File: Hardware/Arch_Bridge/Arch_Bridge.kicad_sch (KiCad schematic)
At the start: 87 parts, among them J1 Conn_01x02, J3 Conn_01x04, J4 Conn_01x04, Q1 2N3904, Q2 MJE2955, Q3 MJE2955, U1 AP63205WU, U11 ESP32-S3-WROOM-1, U12 TXS0102DCT, U13 DRV8231ADDAR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

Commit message: Fixed R11 value, 33k => 3k so that Q2 sources correctly. Tested at 14.5mA on a 12v supply.
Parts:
- R11: value 33k -> 3k; PN RC1206FR-0733KL -> RC1206FR-073KL
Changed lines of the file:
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@@
       (effects (font (size 1.27 1.27)) (justify left))
     )
-    (property "Value" "33k" (at 31.75 168.91 90)
+    (property "Value" "3k" (at 31.75 168.91 90)
       (effects (font (size 1.27 1.27)) (justify left))
     )
@@
       (effects (font (size 1.27 1.27)) hide)
     )
-    (property "PN" "RC1206FR-0733KL" (at 32.385 167.005 0)
+    (property "PN" "RC1206FR-073KL" (at 32.385 167.005 0)
       (effects (font (size 1.27 1.27)) hide)
     )

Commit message: Adjusted R15 value and ADC code to make railsync current source work correctly. 0-208mA availabe.
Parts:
- R15: value 3k -> 470; PN RC1206FR-073KL -> RT1206FRE07470RL
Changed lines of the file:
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@@
       (effects (font (size 1.27 1.27)) (justify left))
     )
-    (property "Value" "3k" (at 185.42 92.71 90)
+    (property "Value" "470" (at 185.42 92.71 90)
       (effects (font (size 1.27 1.27)) (justify left))
     )
@@
       (effects (font (size 1.27 1.27)) hide)
     )
-    (property "PN" "RC1206FR-073KL" (at 182.88 90.17 0)
+    (property "PN" "RT1206FRE07470RL" (at 182.88 90.17 0)
       (effects (font (size 1.27 1.27)) hide)
     )

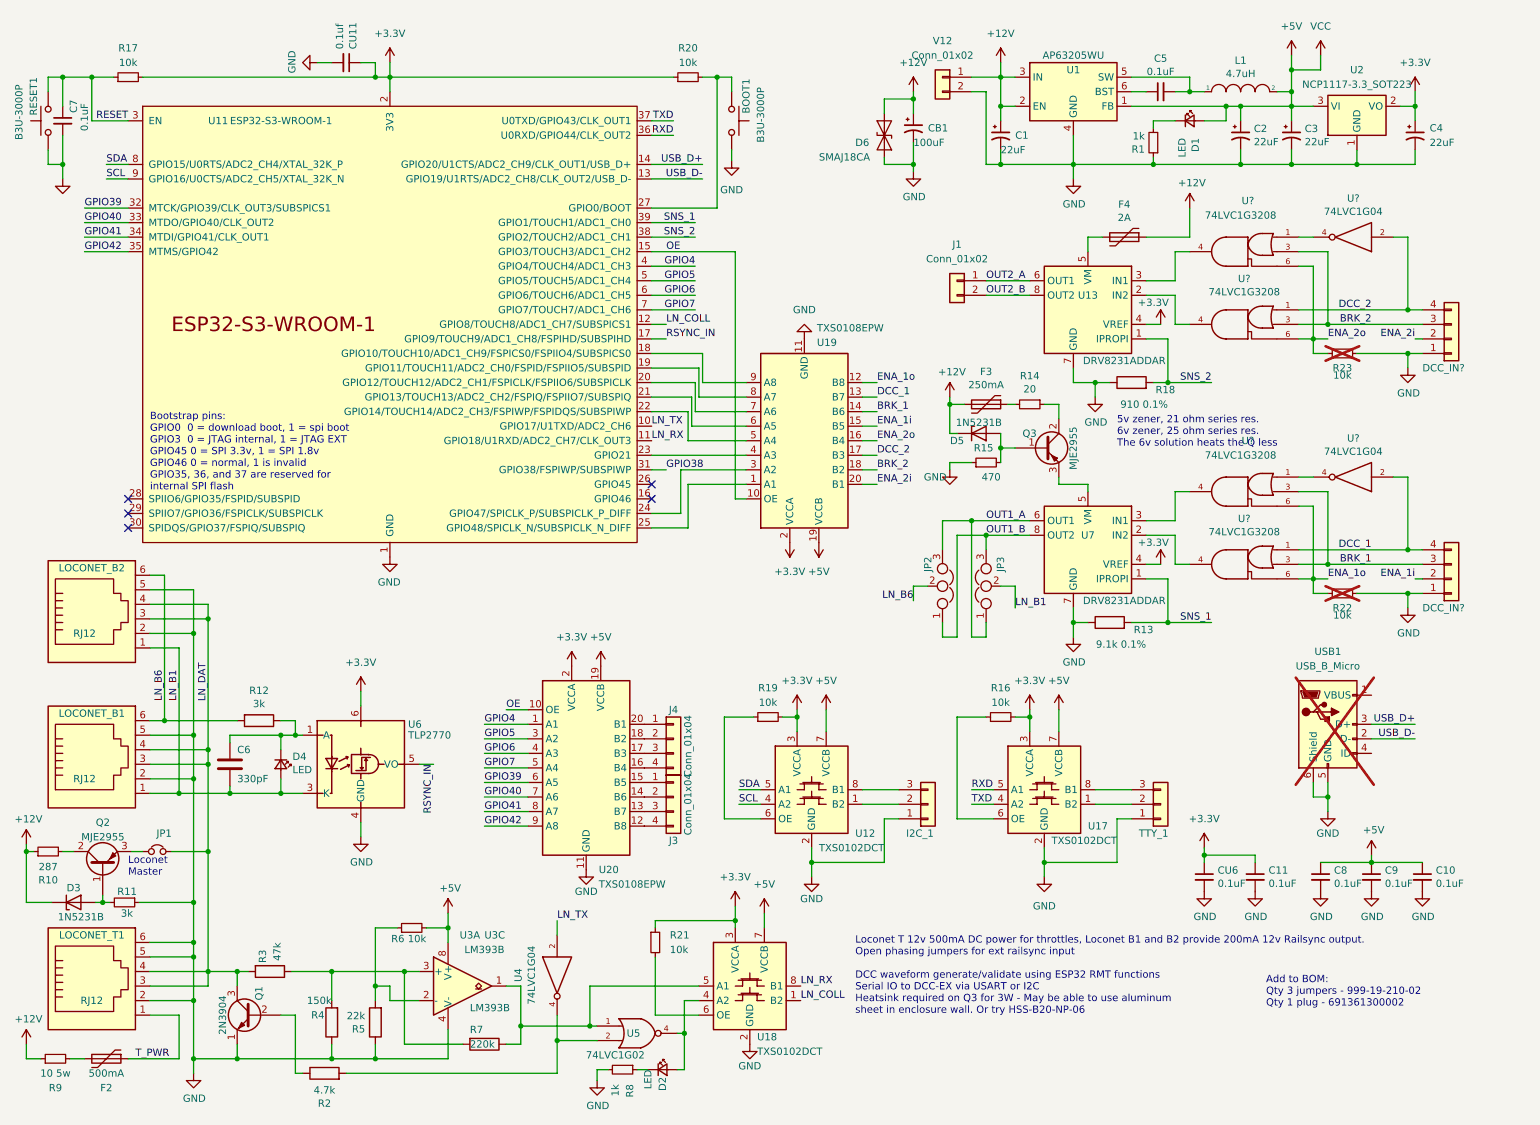
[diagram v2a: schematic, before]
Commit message: Schematic rev 06 with PCB updates. Needs BOM and Fabs reprocessed.
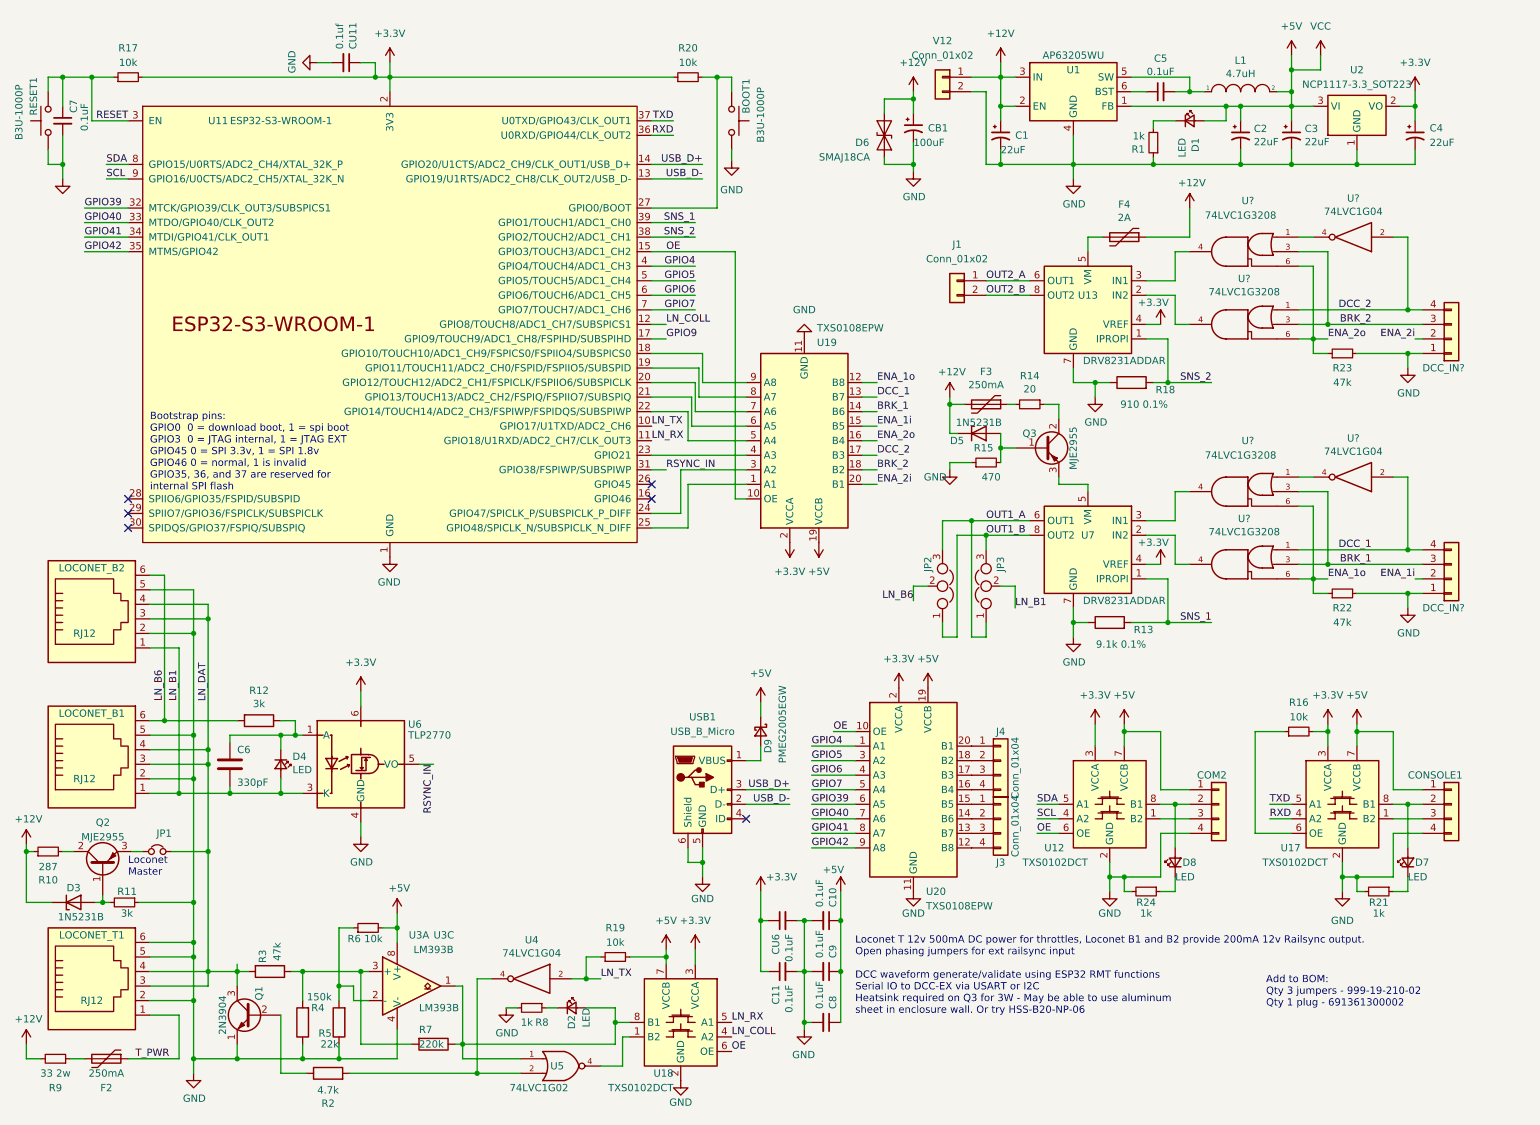
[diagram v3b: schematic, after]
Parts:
- added D7, D8: LED, LED_SMD:LED_1206_3216Metric, symbol Device:LED_Small
- added D9: PMEG2005EGW, Diode_SMD:D_SOD-123, symbol Device:D_Schottky_Small
- added R24: 1k, Resistor_SMD:R_1206_3216Metric, symbol Device:R_Small
- BOOT1, RESET1: value B3U-3000P -> B3U-1000P; footprint Button_Switch_SMD:SW_SPST_B3U-3000P -> Button_Switch_SMD:SW_SPST_B3U-1000P-B; PN B3U-3000P -> B3U-1000P
- COM2: renamed from I2C_1; value Conn_01x03 -> Conn_01x04; footprint Connector_PinSocket_2.54mm:PinSocket_1x03_P2.54mm_Vertical -> Connector_PinSocket_2.54mm:PinSocket_1x04_P2.54mm_Vertical; symbol Connector_Generic:Conn_01x03 -> Connector_Generic:Conn_01x04; PN 929850-01-03-RA -> 929850-01-04-RA
- CONSOLE1: renamed from TTY_1; footprint Connector_PinSocket_2.54mm:PinSocket_1x03_P2.54mm_Vertical -> Connector_PinSocket_2.54mm:PinSocket_1x04_P2.54mm_Vertical; symbol Connector_Generic:Conn_01x03 -> Connector_Generic:Conn_01x04; PN 929850-01-03-RA -> 929850-01-04-RA
- D2, D4: PN 156120RS75300 -> 156120YS75300
- F2: value 500mA -> 250mA; PN PTS120615V050 -> PTS120616V025
- R21: value 10k -> 1k; PN RC1206FR-1310KL -> RC1206FR-071KL
- R22, R23: value 10k -> 47k; PN RC1206FR-1310KL -> RC1206FR-0747KL; now fitted; now in the parts list
- R9: value 10 5w -> 33 2w; footprint Resistor_THT:R_Radial_Power_L13.0mm_W9.0mm_P5.00mm -> Resistor_THT:R_Axial_DIN0414_L11.9mm_D4.5mm_P7.62mm_Vertical; PN SQM500JB-10R -> FMP200JTF52-33R
- USB1: now fitted; now in the parts list
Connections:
- net GPIO38 is gone; now on net RSYNC_IN: U11.31 (GPIO38/FSPIWP/SUBSPIWP)
- net +12V: now also R9.2; no longer R9.1
- net +3.3V: no longer R19.2, R21.1
- net +5V: now also COM2.1 (Pin_1), CONSOLE1.1 (Pin_1), R19.2, D9.1 (K)
- net GND: now also COM2.4 (Pin_4), CONSOLE1.4 (Pin_4), R21.2, R24.2; no longer COM2.1 (Pin_1), CONSOLE1.1 (Pin_1)
- net LN_COLL: now also U18.4 (A2); no longer U18.1 (B2)
- net LN_RX: now also U18.5 (A1); no longer U18.8 (B1)
- net LN_TX: now also R19.1
- net OE: now also U12.6 (OE), U18.6 (OE)
- net RSYNC_IN: no longer U11.17 (GPIO9/TOUCH9/ADC1_CH8/FSPIHD/SUBSPIHD)
- net RXD: now also U17.4 (A2); no longer U17.5 (A1)
- net TXD: now also U17.5 (A1); no longer U17.4 (A2)
- net at R7.1, U3.1, U5.1: now also D2.2 (A), U18.8 (B1); no longer U18.5 (A1)
- net at F2.2: now also R9.1; no longer R9.2
- net at CONSOLE1.2 (Pin_2): now also U17.8 (B1), D7.2 (A); no longer U17.1 (B2)
- net at CONSOLE1.3 (Pin_3): now also U17.1 (B2); no longer U17.8 (B1)
- net at COM2.2 (Pin_2): now also U12.8 (B1), D8.2 (A); no longer U12.1 (B2)
- net at COM2.3 (Pin_3): now also U12.1 (B2); no longer U12.8 (B1)
- net at USB1.1 (VBUS): now also D9.2 (A)
- new net: U18.1 (B2), U5.4
- new net: D7.1 (K), R21.1
- new net: D8.1 (K), R24.1
- new net GPIO9: U11.17 (GPIO9/TOUCH9/ADC1_CH8/FSPIHD/SUBSPIHD)
- no-connect marks 5 -> 6
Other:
- note removed: "5v zener, 21 ohm series res. 6v zener, 25 ohm series res. The 6v solution heats the Q less"
- moved on the sheet: C10, C11, C8, C9, CU6, D2, J3, J4, R16, R2, R4, R5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

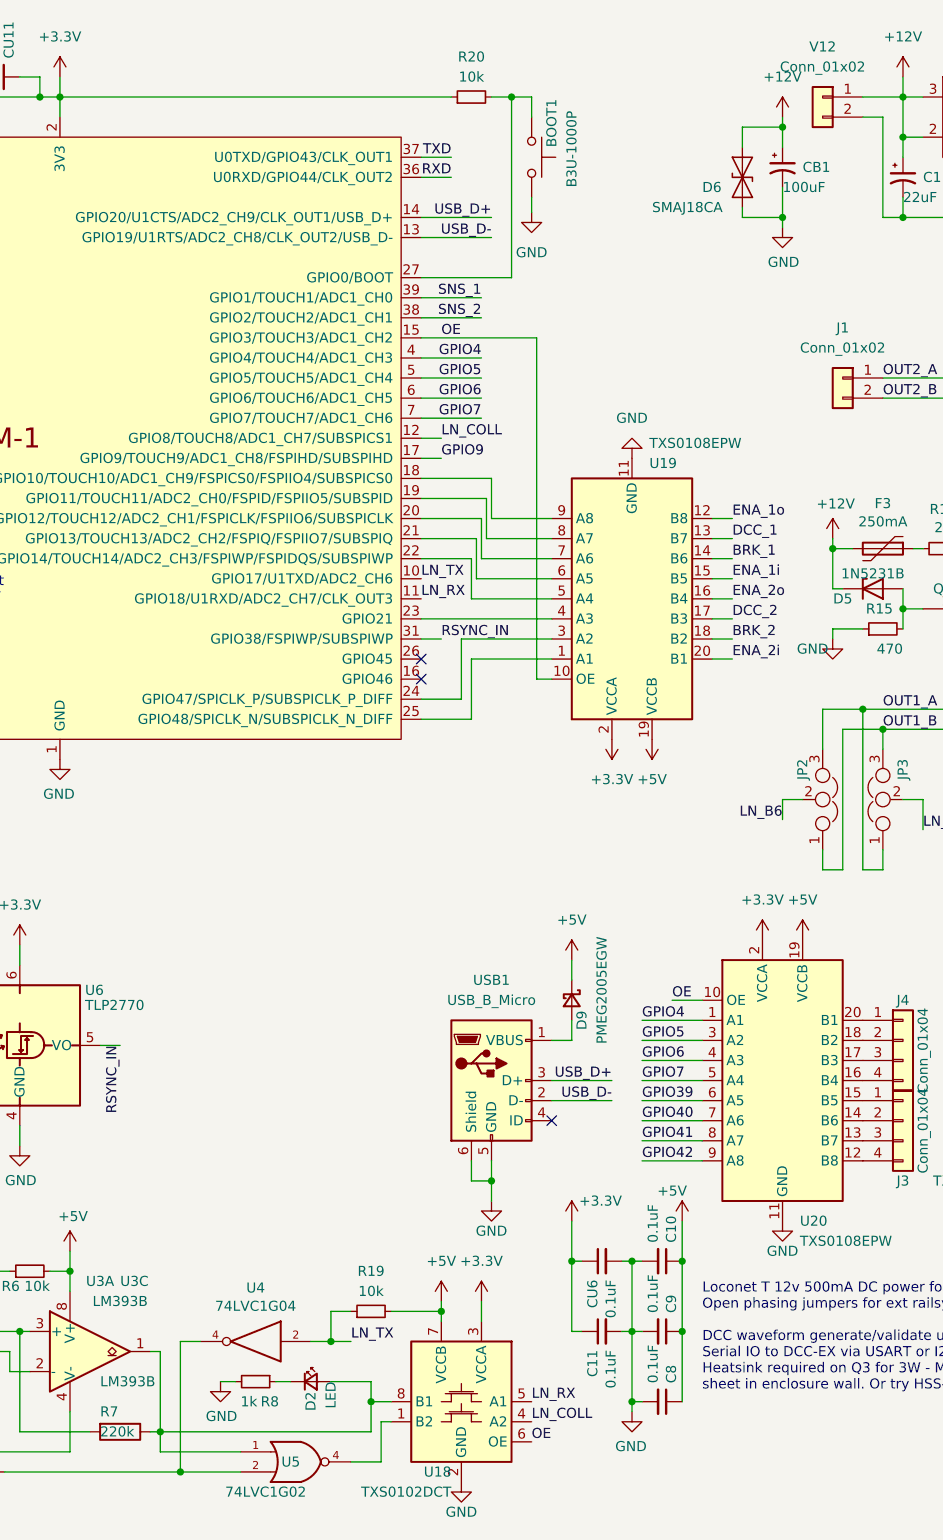
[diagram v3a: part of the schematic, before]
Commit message: Changed CB1 to through hole for field installaion, no longer in BOM or populated by default.
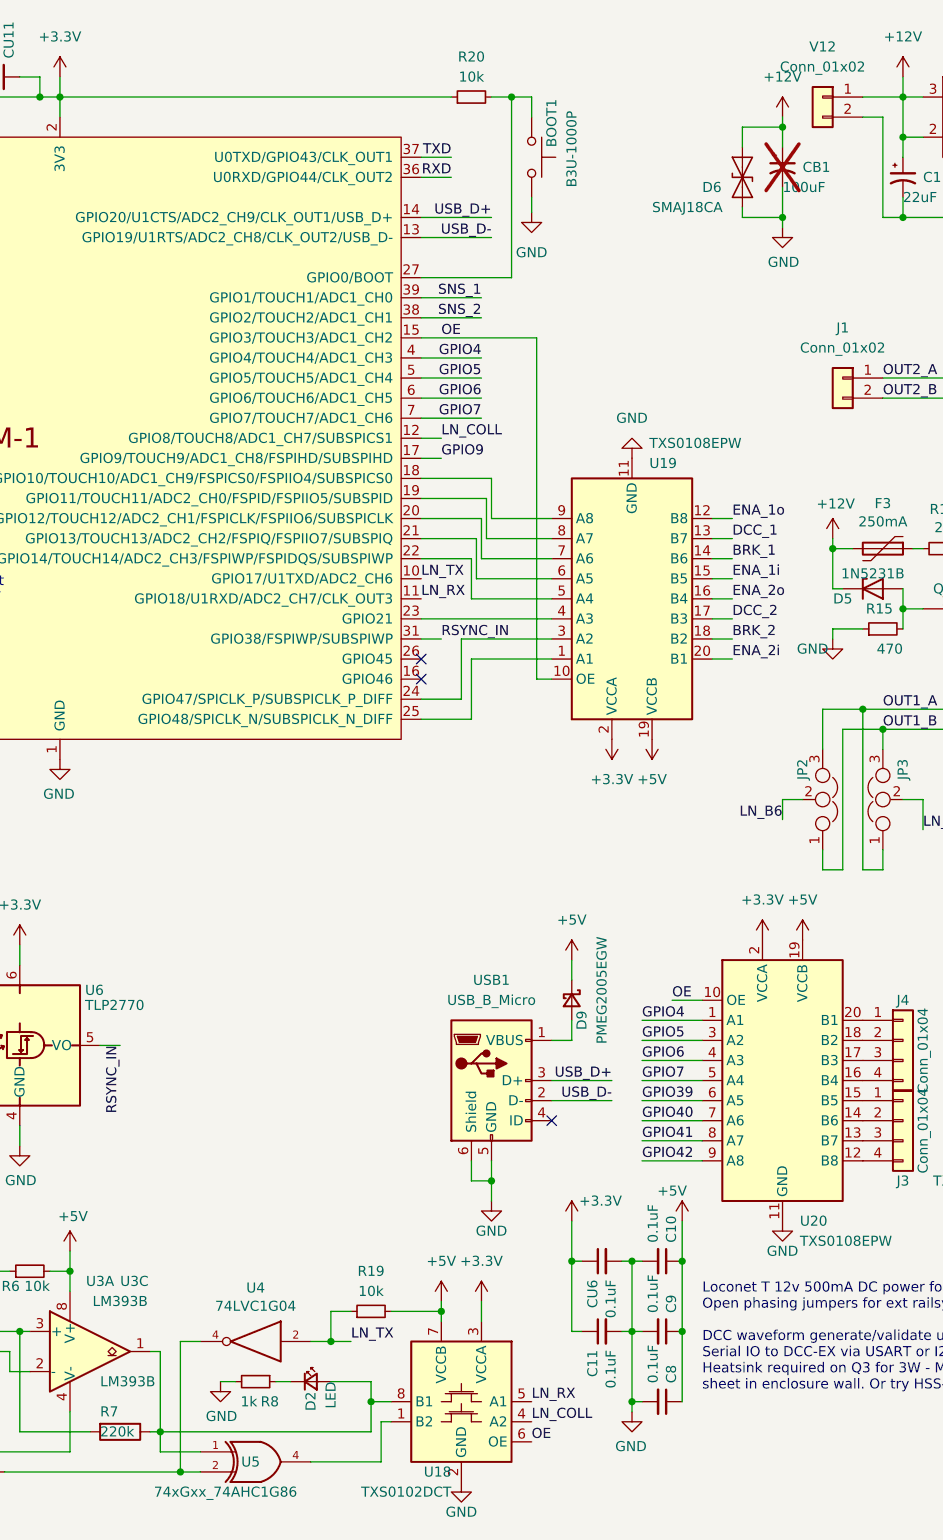
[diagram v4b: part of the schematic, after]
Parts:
- CB1: footprint Capacitor_SMD:CP_Elec_6.3x7.7 -> Capacitor_THT:CP_Radial_D6.3mm_P2.50mm; PN 865080545012 -> 860020573008; now not fitted; now left out of the parts list
- U5: value 74LVC1G02 -> 74xGxx_74AHC1G86; symbol Loconet DCC Interface ESP32-rescue:74AHCT1G02-74xGxx -> Loconet DCC Interface-rescue:74AHC1G86-74xGxx
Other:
- moved on the sheet: U5
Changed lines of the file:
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@@
   (junction (at 157.48 170.18) (diameter 0) (color 0 0 0 0)
   )
+  (junction (at 93.98 196.85) (diameter 0) (color 0 0 0 0)
+  )
   (junction (at 44.45 120.015) (diameter 0) (color 0 0 0 0)
   )
@@
   (junction (at 236.22 27.94) (diameter 0) (color 0 0 0 0)
   )
-  (junction (at 93.98 196.85) (diameter 0) (color 0 0 0 0)
-  )
   (junction (at 127 176.53) (diameter 0) (color 0 0 0 0)
   )
@@
     (stroke (width 0) (type default))
   )
+  (wire (pts (xy 91.44 194.31) (xy 96.52 194.31))
+    (stroke (width 0) (type default))
+  )
   (wire (pts (xy 36.83 184.15) (xy 44.45 184.15))
     (stroke (width 0) (type default))
@@
     (stroke (width 0) (type default))
   )
-  (wire (pts (xy 93.98 196.85) (xy 101.6 196.85))
-    (stroke (width 0) (type default))
-  )
   (wire (pts (xy 132.715 78.74) (xy 132.715 73.66))
     (stroke (width 0) (type default))
@@
     (stroke (width 0) (type default))
   )
-  (wire (pts (xy 115.57 195.58) (xy 119.38 195.58))
+  (wire (pts (xy 110.49 195.58) (xy 119.38 195.58))
     (stroke (width 0) (type default))
   )
@@
     (stroke (width 0) (type default))
   )
-  (wire (pts (xy 91.44 194.31) (xy 101.6 194.31))
-    (stroke (width 0) (type default))
-  )
   (wire (pts (xy 107.95 185.42) (xy 106.045 185.42))
     (stroke (width 0) (type default))
@@
     (stroke (width 0) (type default))
   )
+  (wire (pts (xy 93.98 196.85) (xy 96.52 196.85))
+    (stroke (width 0) (type default))
+  )
   (wire (pts (xy 237.49 107.95) (xy 242.57 107.95))
     (stroke (width 0) (type default))
@@
     )
   )
-  (symbol (lib_id "Loconet DCC Interface ESP32-rescue:74AHCT1G02-74xGxx") (at 109.22 195.58 0) (unit 1)
+  (symbol (lib_id "Loconet DCC Interface-rescue:74AHC1G86-74xGxx") (at 104.14 195.58 0) (unit 1)
     (in_bom yes) (on_board yes) (dnp no)
-    (property "Reference" "U5" (at 107.95 195.58 0)
+    (property "Reference" "U5" (at 102.87 195.58 0)
       (effects (font (size 1.27 1.27)))
     )
-    (property "Value" "74LVC1G02" (at 104.775 199.39 0)
+    (property "Value" "74xGxx_74AHC1G86" (at 99.695 199.39 0)
       (effects (font (size 1.27 1.27)))
     )
-    (property "Footprint" "Package_TO_SOT_SMD:SOT-23-5_HandSoldering" (at 109.22 195.58 0)
+    (property "Footprint" "Package_TO_SOT_SMD:SOT-23-5_HandSoldering" (at 104.14 195.58 0)
       (effects (font (size 1.27 1.27)) hide)
     )
-    (property "Datasheet" "http://www.ti.com/lit/sg/scyt129e/scyt129e.pdf" (at 109.22 195.58 0)
+    (property "Datasheet" "http://www.ti.com/lit/sg/scyt129e/scyt129e.pdf" (at 104.14 195.58 0)
       (effects (font (size 1.27 1.27)) hide)
     )
-    (property "PN" "SN74LVC1G02DBVR" (at 109.22 195.58 0)
+    (property "PN" "SN74LVC1G02DBVR" (at 104.14 195.58 0)
       (effects (font (size 1.27 1.27)) hide)
     )
-    (property "MFG" "Texas Insturments" (at 109.22 195.58 0)
+    (property "MFG" "Texas Insturments" (at 104.14 195.58 0)
       (effects (font (size 1.27 1.27)) hide)
     )
@@
   )
   (symbol (lib_id "Device:C_Polarized_Small_US") (at 170.18 31.75 0) (unit 1)
-    (in_bom yes) (on_board yes) (dnp no)
+    (in_bom no) (on_board yes) (dnp yes)
     (property "Reference" "CB1" (at 172.72 31.75 0)
       (effects (font (size 1.27 1.27)) (justify left))
@@
       (effects (font (size 1.27 1.27)) (justify left))
     )
-    (property "Footprint" "Capacitor_SMD:CP_Elec_6.3x7.7" (at 170.18 31.75 0)
+    (property "Footprint" "Capacitor_THT:CP_Radial_D6.3mm_P2.50mm" (at 170.18 31.75 0)
       (effects (font (size 1.27 1.27)) hide)
     )
@@
       (effects (font (size 1.27 1.27)) hide)
     )
-    (property "PN" "865080545012" (at 170.18 31.75 0)
+    (property "PN" "860020573008" (at 170.18 31.75 0)
       (effects (font (size 1.27 1.27)) hide)
     )
